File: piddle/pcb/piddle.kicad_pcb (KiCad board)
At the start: 2 copper layers, 133.5 x 118 mm, 68 parts, among them J1 Conn_01x03_Socket, J10 Conn_01x03_Socket, J11 Conn_01x02_Socket, J12 Conn_01x02_Socket, J13 Conn_01x02_Pin, J2 Conn_01x03_Socket, J3 Conn_01x03_Socket, J4 Conn_01x03_Socket, J5 Conn_01x03_Socket, J6 Conn_01x03_Socket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

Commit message: Gerber stuff
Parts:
- J1: footprint Connector_JST:JST_PH_S3B-PH-K_1x03_P2.00mm_Horizontal -> Connector_PinSocket_2.54mm:PinSocket_1x03_P2.54mm_Vertical
- moved J1 1.48 mm to (102.1, 69.1), turned to -90 degrees
- renumbered J6 to locked
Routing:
- net Net-(J1-Pin_3): track 10.1 -> 14.8 mm
- net GND: track 38.1 -> 41.4 mm
- net Net-(D1-DOUT): track 5.24 -> 4.28 mm
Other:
- board text added: "GPIO4"

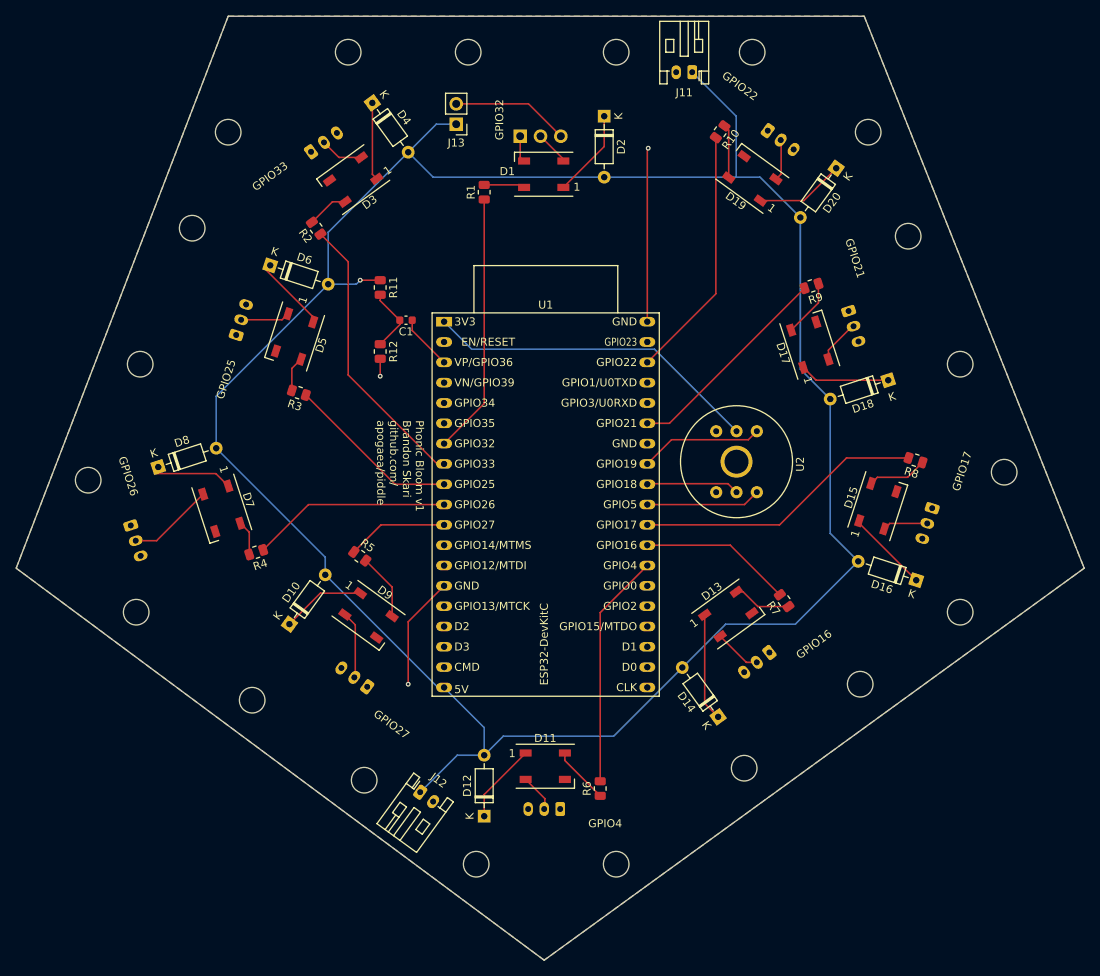
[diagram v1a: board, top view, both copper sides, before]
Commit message: Switch to plain through holes for LED strip connections
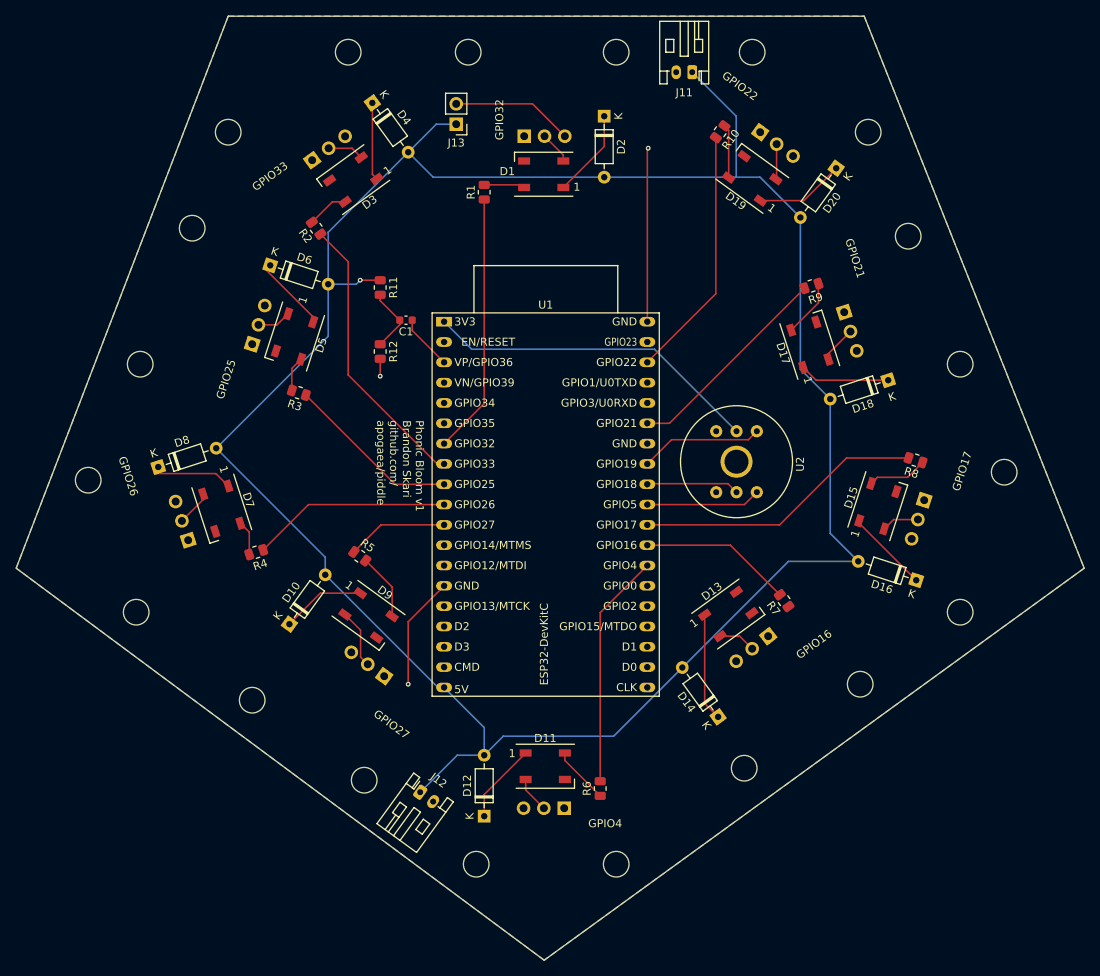
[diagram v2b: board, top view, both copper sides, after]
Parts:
- J1: footprint Connector_PinSocket_2.54mm:PinSocket_1x03_P2.54mm_Vertical -> Connector_PinHeader_2.54mm:PinHeader_1x03_P2.54mm_Vertical
- J10, J2, J3, J4, J5, J7, J8, J9, locked: footprint Connector_JST:JST_PH_S3B-PH-K_1x03_P2.00mm_Horizontal -> Connector_PinHeader_2.54mm:PinHeader_1x03_P2.54mm_Vertical
- moved J4 7.41 mm to (60.6, 119.6), turned to 18 degrees
- moved J5 2.50 mm to (85.1, 136.6), turned to 54 degrees
- moved J3 2.31 mm to (68.6, 95.1), turned to -18 degrees
- moved J7 2.04 mm to (133.1, 131.6), turned to 128 degrees
- moved J8 1.41 mm to (152.6, 114.6), turned to 162 degrees
- moved J2 1.06 mm to (76.1, 72.1), turned to -54 degrees
- moved J10 0.96 mm to (132.1, 68.6), turned to -126 degrees
- moved J9 0.57 mm to (142.6, 91.1), turned to -162 degrees
- moved locked 0.51 mm to (107.6, 153.1), turned to 90 degrees
- moved J1 0.50 mm to (102.6, 69.1)
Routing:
- net Net-(D13-DIN): track 7.27 -> 0.00 mm
- net Net-(D7-DOUT): track 10.8 -> 4.44 mm
- net GND: track 41.4 -> 38.1 mm
- net Net-(D5-DOUT): track 6.18 -> 4.28 mm
- net Net-(D13-DOUT): track 5.93 -> 4.65 mm
- net Net-(D19-DOUT): track 5.48 -> 4.42 mm
- net Net-(D15-DOUT): track 5.65 -> 4.69 mm
- net Net-(D3-DOUT): track 5.44 -> 4.56 mm
- net Net-(D9-DOUT): track 8.07 -> 7.40 mm
- net Net-(J1-Pin_3): track 14.8 -> 15.3 mm

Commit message: e through hole resistors
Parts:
- R1, R10, R11, R12, R2, R3, R4, R5, R6, R7, R8, R9: footprint Resistor_SMD:R_0805_2012Metric -> Resistor_THT:R_Axial_DIN0207_L6.3mm_D2.5mm_P10.16mm_Horizontal
- moved R7 8.36 mm to (140.1, 133.8)
- moved R9 7.42 mm to (145.6, 85.6)
- moved R8 5.80 mm to (157.0, 111.5)
- moved R12 5.51 mm to (84.6, 101.5)
- moved R6 3.86 mm to (112.1, 154.5)
- moved R10 3.16 mm to (129.1, 66.1)
- moved R5 2.79 mm to (80.1, 119.6)
- moved D9 2.78 mm to (85.6, 130.3)
- moved R1 1.67 mm to (98.1, 74.5)
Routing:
- net /GPIO33: track 35.6 -> 0.87 mm
- net /GPIO25: track 21.9 -> 0.00 mm
- net Net-(D13-DIN): track 0.00 -> 14.2 mm
- net GND: track 38.1 -> 25.3 mm, vias 3 -> 2
- net Net-(D1-DIN): track 5.62 -> 15.7 mm
- net /GPIO22: track 31.6 -> 25.2 mm
- net Net-(D3-DIN): track 5.21 -> 11.6 mm
- net Net-(D7-DIN): track 4.36 -> 10.5 mm
- net Net-(D5-DIN): track 4.39 -> 10.4 mm
- net Net-(D17-DIN): track 7.22 -> 12.8 mm
- net /GPIO4: track 29.4 -> 24.0 mm
- net Net-(D15-DIN): track 7.48 -> 11.4 mm
- net Net-(D9-DIN): track 8.33 -> 4.95 mm
- net Net-(D11-DIN): track 7.18 -> 10.1 mm
- net /GPIO17: track 36.1 -> 33.2 mm
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
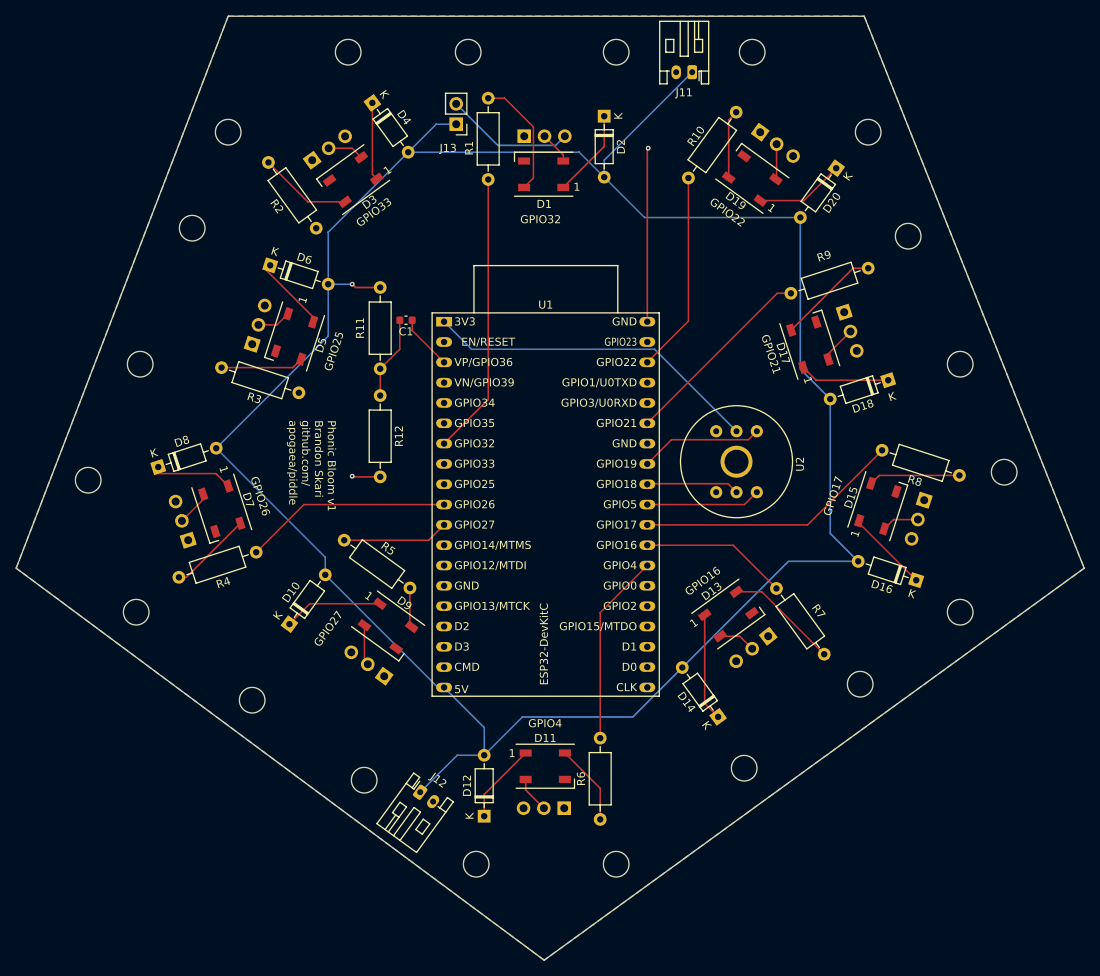
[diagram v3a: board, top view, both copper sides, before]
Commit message: Make diodes through hole
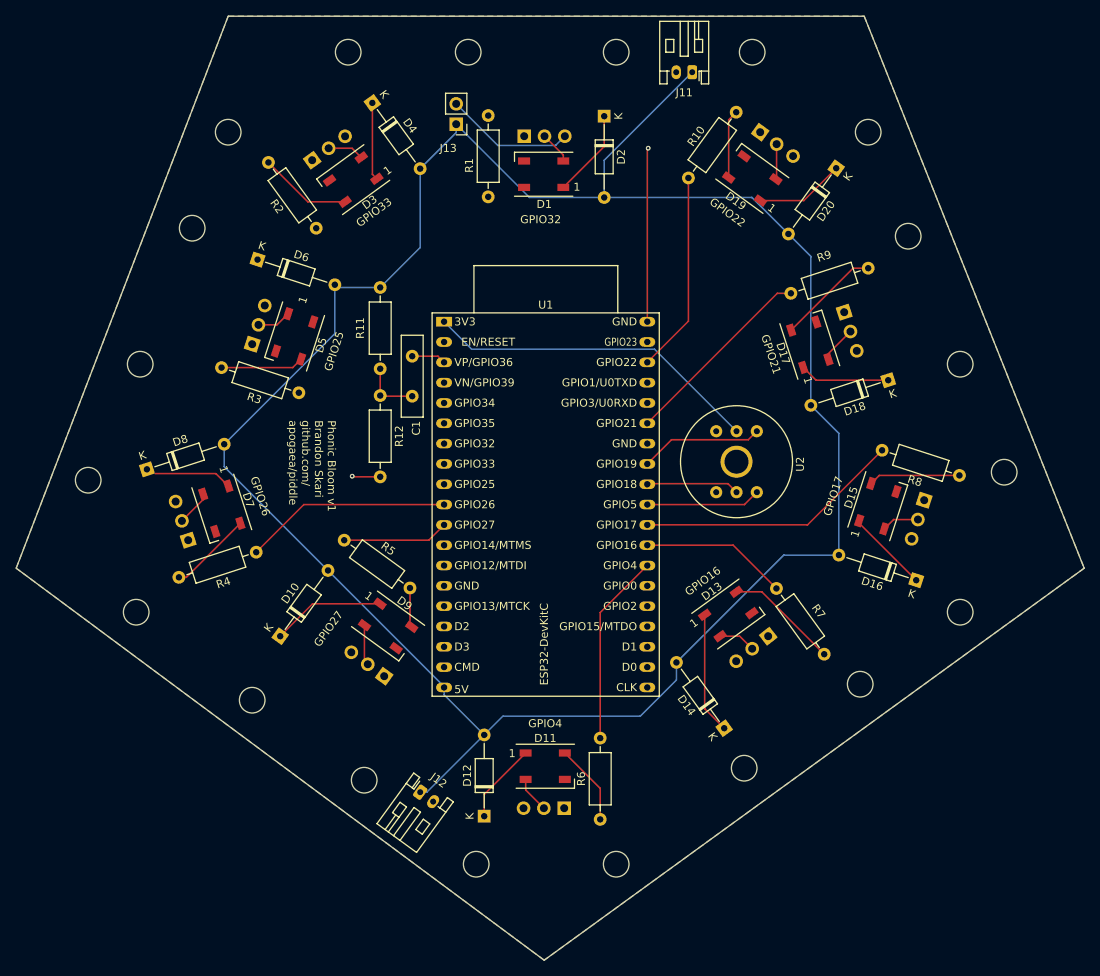
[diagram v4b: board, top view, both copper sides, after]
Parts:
- C1: footprint Capacitor_SMD:C_0603_1608Metric -> Capacitor_THT:C_Disc_D10.0mm_W2.5mm_P5.00mm
- D10, D12, D14, D16, D18, D2, D20, D4, D6, D8: footprint Diode_THT:D_DO-35_SOD27_P7.62mm_Horizontal -> Diode_THT:D_DO-35_SOD27_P10.16mm_Horizontal
- moved C1 4.57 mm to (88.6, 96.6), turned to -90 degrees
- moved R1 2.17 mm to (98.1, 76.7)
- moved D10 1.90 mm to (72.1, 131.6)
- moved D6 1.74 mm to (69.3, 84.5)
- moved D14 1.61 mm to (127.6, 143.1)
- moved D8 1.44 mm to (55.5, 110.7)
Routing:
- net /GPIO32: track 35.3 -> 0.00 mm
- net Net-(D1-DIN): track 15.7 -> 0.50 mm
- net +5V: track 297.0 -> 282.5 mm, vias 1 -> 0
- net Net-(D5-VDD): track 9.11 -> 0.61 mm
- net Net-(C1-Pad2): track 10.4 -> 7.38 mm
- net /GPIO36: track 6.92 -> 4.30 mm
- net Net-(D10-K): track 12.4 -> 14.2 mm
- net Net-(D13-VDD): track 13.4 -> 15.2 mm

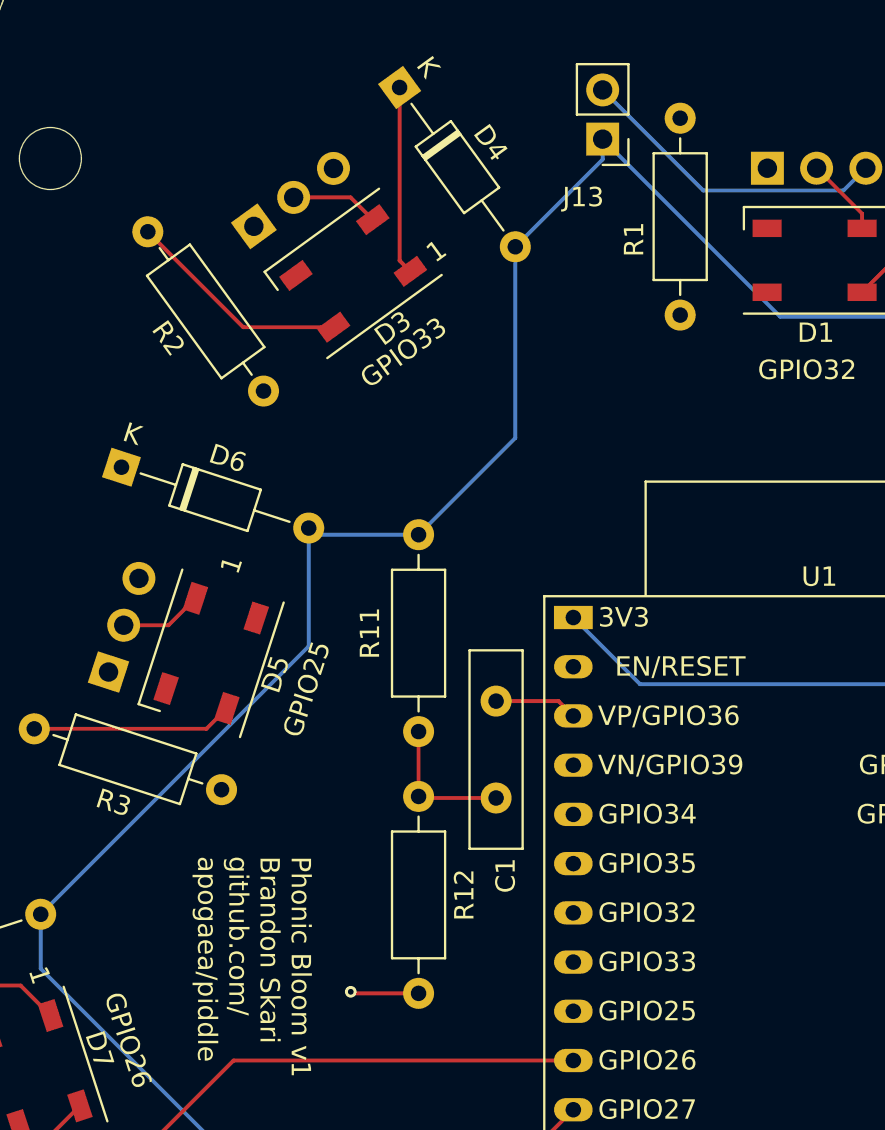
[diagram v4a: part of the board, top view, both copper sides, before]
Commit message: Fix some missed connections. DRC is happy now!
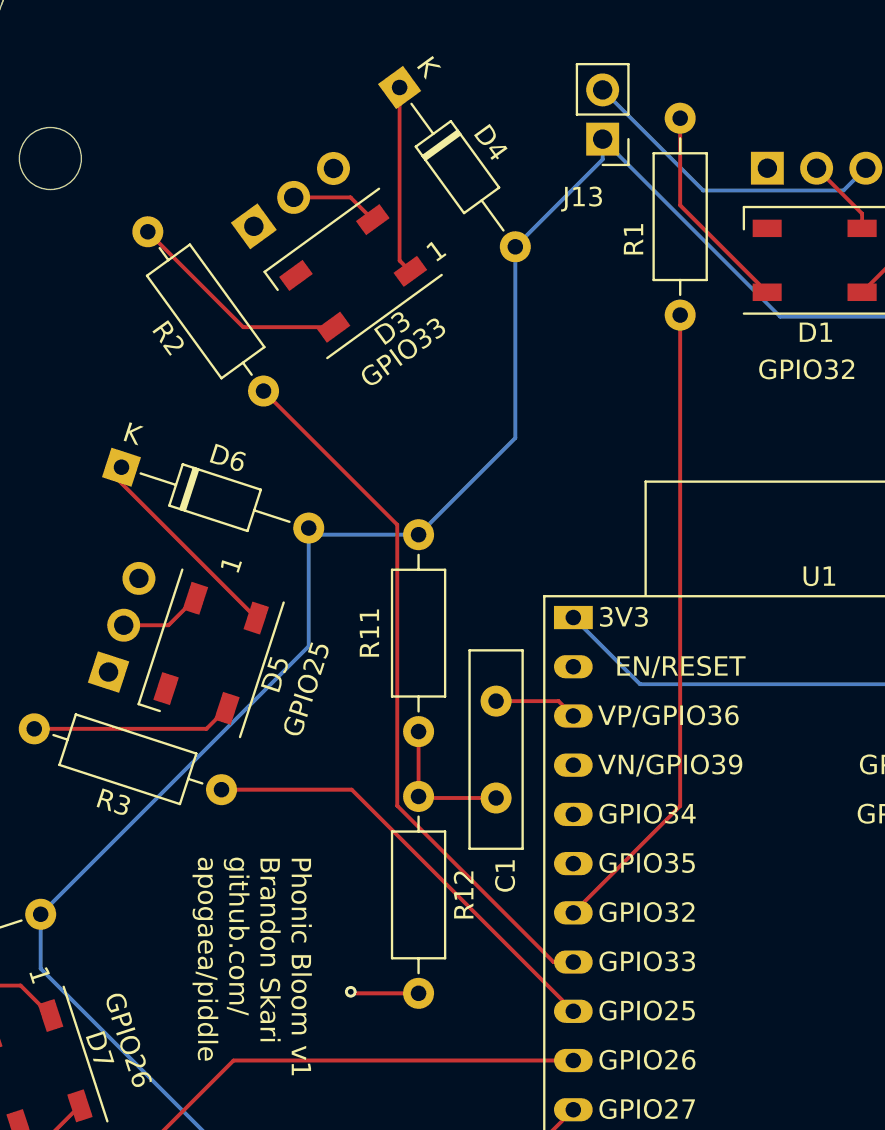
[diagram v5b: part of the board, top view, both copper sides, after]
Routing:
- net /GPIO33: track 0.87 -> 36.7 mm
- net /GPIO32: track 0.00 -> 33.1 mm
- net /GPIO25: track 0.00 -> 22.9 mm
- net Net-(D5-VDD): track 0.61 -> 11.5 mm
- net Net-(D1-DIN): track 0.50 -> 11.3 mm
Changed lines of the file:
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@@
   (segment (start 91.833623 96.596343) (end 92.6 97.36272) (width 0.2) (layer "F.Cu") (net 3))
   (segment (start 88.61328 96.596343) (end 91.833623 96.596343) (width 0.2) (layer "F.Cu") (net 3))
+  (segment (start 81.163429 101.166149) (end 92.6 112.60272) (width 0.2) (layer "F.Cu") (net 7))
+  (segment (start 74.444647 101.166149) (end 81.163429 101.166149) (width 0.2) (layer "F.Cu") (net 7))
   (segment (start 69.11328 121.096343) (end 75.066903 115.14272) (width 0.2) (layer "F.Cu") (net 8))
   (segment (start 75.066903 115.14272) (end 92.6 115.14272) (width 0.2) (layer "F.Cu") (net 8))
@@
   (segment (start 99.30328 70.246343) (end 94.11328 65.056343) (width 0.2) (layer "B.Cu") (net 37))
   (segment (start 107.69328 69.096343) (end 106.54328 70.246343) (width 0.2) (layer "B.Cu") (net 37))
+  (segment (start 92.6 107.52272) (end 98.11328 102.00944) (width 0.2) (layer "F.Cu") (net 38))
+  (segment (start 98.11328 102.00944) (end 98.11328 76.676343) (width 0.2) (layer "F.Cu") (net 38))
   (segment (start 83.634356 64.931634) (end 83.634356 73.864421) (width 0.2) (layer "F.Cu") (net 39))
   (segment (start 83.634356 73.864421) (end 84.189691 74.419756) (width 0.2) (layer "F.Cu") (net 39))
   (segment (start 78.168183 70.603368) (end 81.103368 70.603368) (width 0.2) (layer "F.Cu") (net 40))
   (segment (start 81.103368 70.603368) (end 82.25 71.75) (width 0.2) (layer "F.Cu") (net 40))
-  (segment (start 91.732792 110.06272) (end 92.6 110.06272) (width 0.2) (layer "F.Cu") (net 41))
+  (segment (start 76.61328 80.596343) (end 83.51328 87.496343) (width 0.2) (layer "F.Cu") (net 41))
+  (segment (start 83.51328 101.996343) (end 91.579657 110.06272) (width 0.2) (layer "F.Cu") (net 41))
+  (segment (start 91.579657 110.06272) (end 92.6 110.06272) (width 0.2) (layer "F.Cu") (net 41))
+  (segment (start 83.51328 87.496343) (end 83.51328 101.996343) (width 0.2) (layer "F.Cu") (net 41))
+  (segment (start 69.281913 84.526537) (end 69.183086 84.526537) (width 0.2) (layer "F.Cu") (net 42))
+  (segment (start 69.11328 84.596343) (end 69.11328 85.187246) (width 0.2) (layer "F.Cu") (net 42))
+  (segment (start 69.11328 85.187246) (end 76.236666 92.310632) (width 0.2) (layer "F.Cu") (net 42))
+  (segment (start 69.183086 84.526537) (end 69.11328 84.596343) (width 0.2) (layer "F.Cu") (net 42))
   (segment (start 76.236666 91.702792) (end 76.236666 92.310632) (width 0.2) (layer "F.Cu") (net 42))
   (segment (start 71.708395 92.680659) (end 73.098179 91.290875) (width 0.2) (layer "F.Cu") (net 43))
@@
   (segment (start 141.61328 73.096343) (end 137.563376 77.146247) (width 0.2) (layer "F.Cu") (net 66))
   (segment (start 102.096937 75.5) (end 102.6 75.5) (width 0.2) (layer "F.Cu") (net 67))
+  (segment (start 98.11328 71.01328) (end 102.6 75.5) (width 0.2) (layer "F.Cu") (net 67))
+  (segment (start 98.11328 66.516343) (end 98.11328 71.01328) (width 0.2) (layer "F.Cu") (net 67))
   (segment (start 75.564556 77.299904) (end 80.225508 77.299904) (width 0.2) (layer "F.Cu") (net 68))
   (segment (start 70.641382 72.37673) (end 75.564556 77.299904) (width 0.2) (layer "F.Cu") (net 68))
